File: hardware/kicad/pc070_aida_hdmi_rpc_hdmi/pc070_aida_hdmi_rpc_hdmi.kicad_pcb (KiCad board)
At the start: 4 copper layers, 40 x 150 mm, 16 parts, among them J1 HDMR-19-01-S-SM-TR, J10 HDMR-19-01-S-SM-TR, J11 HDMR-19-01-S-SM-TR, J12 HDMR-19-01-S-SM-TR, J2 HDMR-19-01-S-SM-TR, J3 HDMR-19-01-S-SM-TR, J4 HDMR-19-01-S-SM-TR, J5 HDMR-19-01-S-SM-TR, J6 HDMR-19-01-S-SM-TR, J7 HDMR-19-01-S-SM-TR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

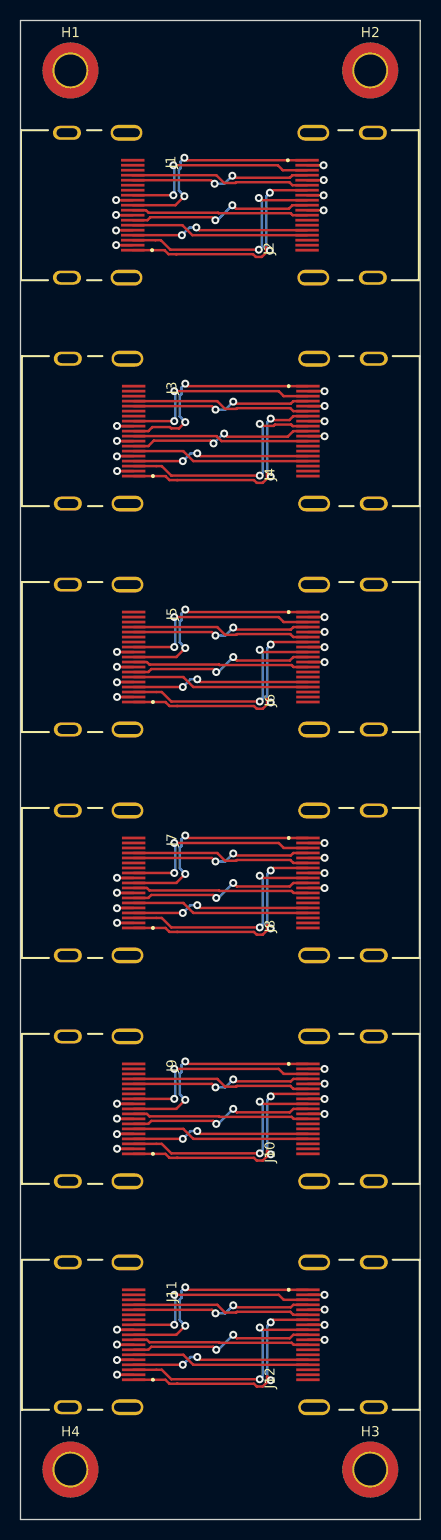
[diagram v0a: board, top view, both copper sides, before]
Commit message: Tweaked 3D model alignment on HDMI connector
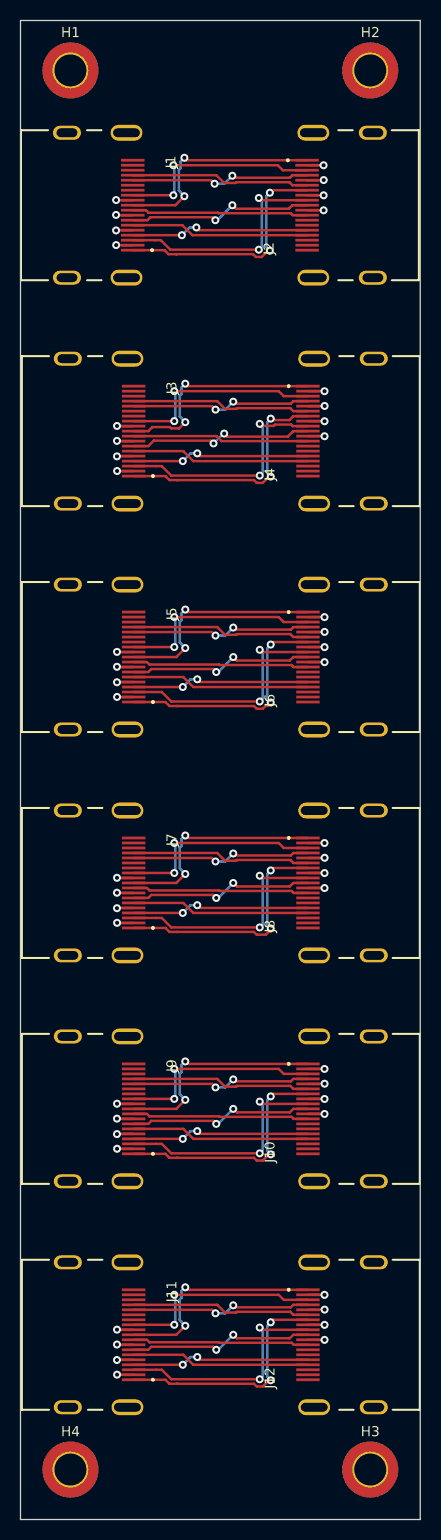
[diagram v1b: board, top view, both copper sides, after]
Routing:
- net /pc070_aida_hdmi_rpc_hdmi_single1/BUSY: track 25.0 -> 24.4 mm
- net /pc070_aida_hdmi_rpc_hdmi_single3/BUSY: track 24.9 -> 24.3 mm
- net /pc070_aida_hdmi_rpc_hdmi_single/BUSY: track 24.9 -> 24.3 mm
- net /pc070_aida_hdmi_rpc_hdmi_single5/BUSY: track 24.9 -> 24.3 mm
- net /pc070_aida_hdmi_rpc_hdmi_single2/BUSY: track 24.9 -> 24.3 mm
- net /pc070_aida_hdmi_rpc_hdmi_single4/BUSY: track 24.9 -> 24.4 mm
